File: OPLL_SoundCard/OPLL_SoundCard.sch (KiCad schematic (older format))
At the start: 19 parts, among them P1 Digital, P10 CONN_01X01, P11 CONN_01X01, P12 CONN_01X01, P13 CONN_01X01, P2 Power, P3 Analog, P4 Analog, P5 PWM, P6 PWM, P7 Communication, P8 CONN_01X01, P9 CONN_01X01

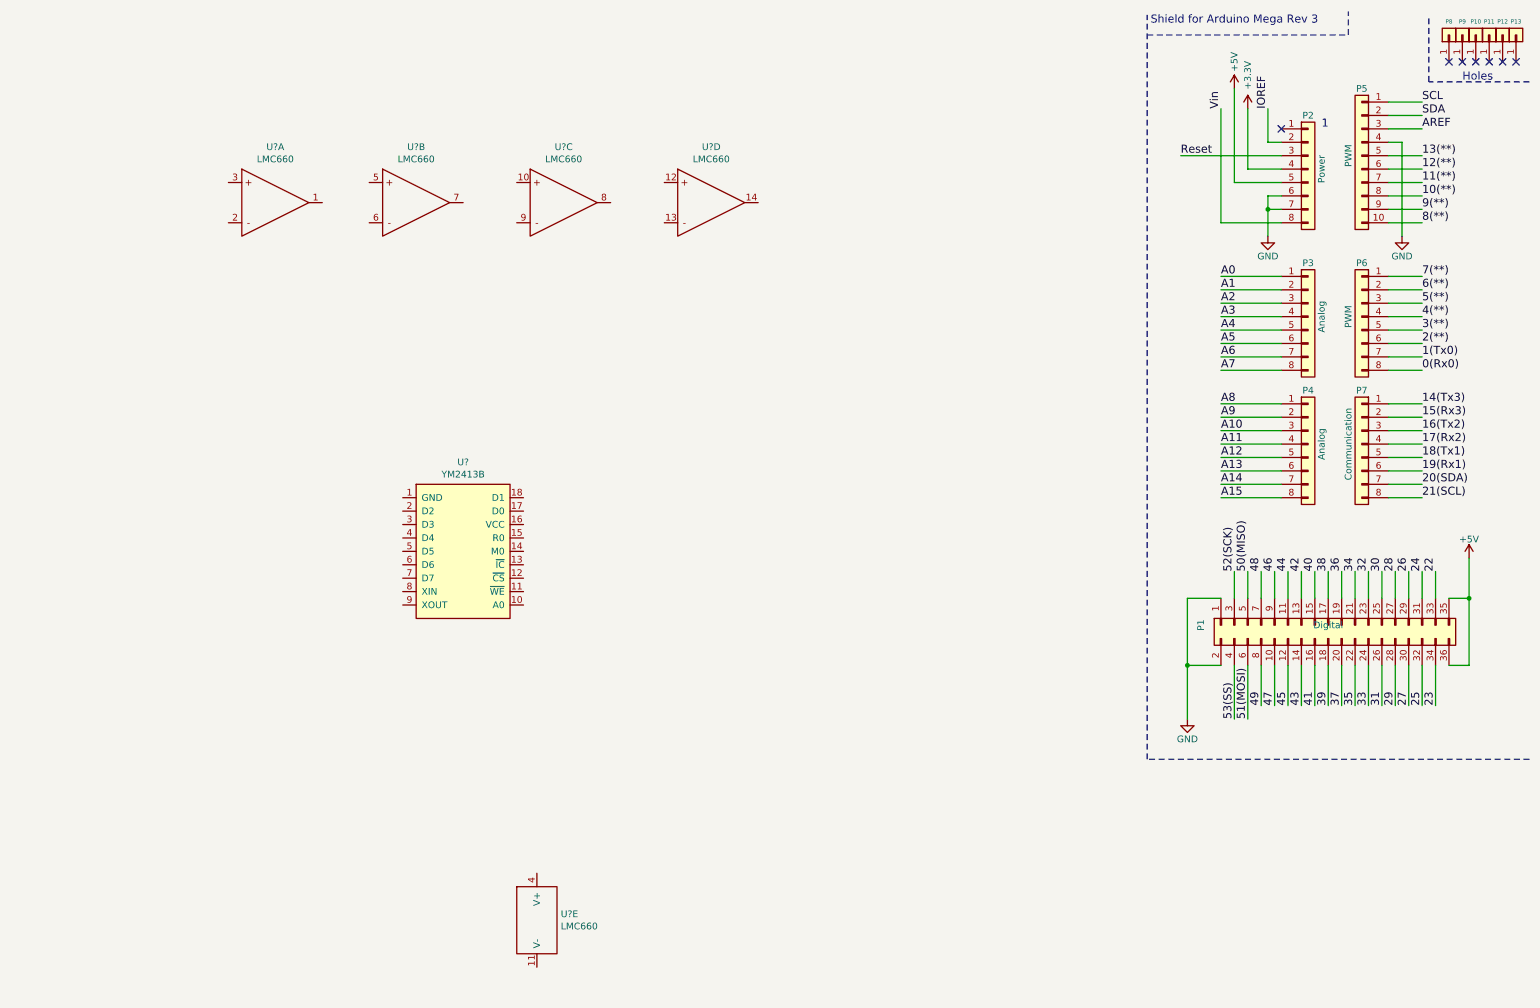
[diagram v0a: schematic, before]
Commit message: 15.12.2020 - Lecture - OPLL schema done
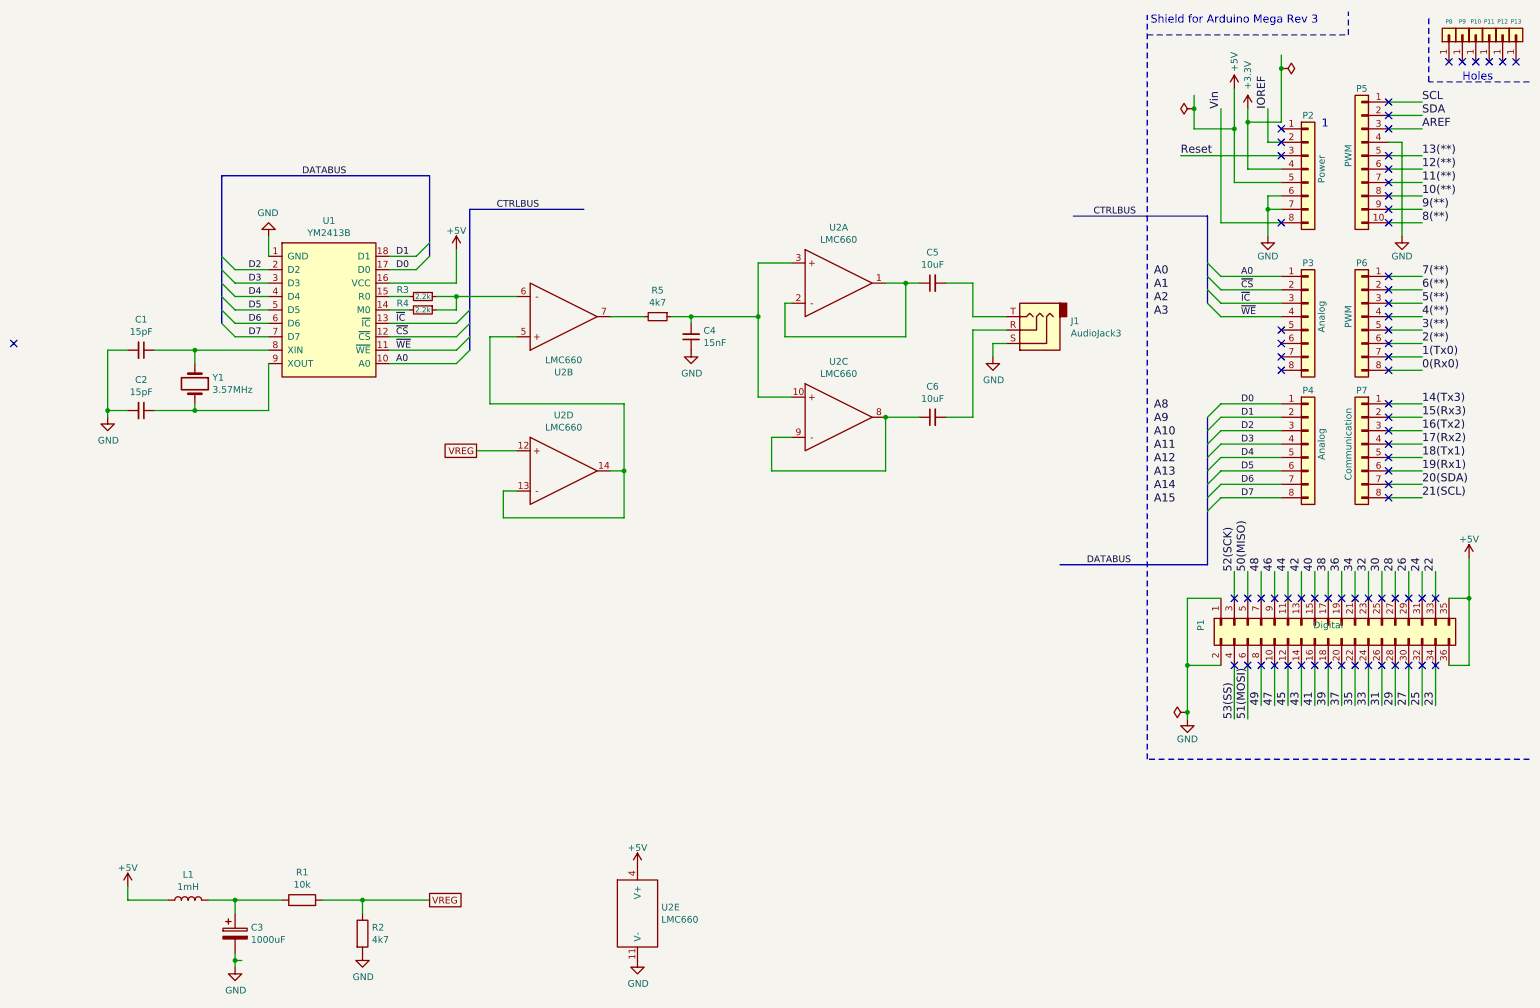
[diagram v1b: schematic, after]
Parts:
- removed U?: LMC660, Package_SO:SOIC-14_3.9x8.7mm_P1.27mm, symbol LMC:LMC660
- added C1, C2: 15pF, symbol Device:C_Small
- added C3: 1000uF, symbol Device:CP
- added C4: 15nF, symbol Device:C_Small
- added C5, C6: 10uF, symbol Device:C_Small
- added J1: AudioJack3, symbol Connector:AudioJack3
- added L1: 1mH, symbol Device:L
- added R1: 10k, symbol Device:R
- added R2: 4k7, symbol Device:R
- added R3, R4: 2.2k, symbol Device:R_Small
- added R5: 4k7, symbol Device:R_Small
- added unit 3 of U2
- added Y1: 3.57MHz, symbol Device:Crystal
- gave numbers to parts that had none: 2
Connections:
- net +5V: now also U1.16 (VCC), U2.4 (V+), L1.1
- net A0: now also U1.10 (A0)
- net A1: no longer P3.2 (Pin_2)
- net A10: no longer P4.3 (Pin_3)
- net A11: no longer P4.4 (Pin_4)
- net A12: no longer P4.5 (Pin_5)
- net A13: no longer P4.6 (Pin_6)
- net A14: no longer P4.7 (Pin_7)
- net A15: no longer P4.8 (Pin_8)
- net A2: no longer P3.3 (Pin_3)
- net A3: no longer P3.4 (Pin_4)
- net A8: no longer P4.1 (Pin_1)
- net A9: no longer P4.2 (Pin_2)
- net GND: now also U1.1 (GND), U2.11 (V-), C1.2, C2.2, C3.2, C4.1, J1.S, R2.2
- net at U2.1: now also U2.2, C5.1
- net at U2.3: now also C4.2, R5.1, U2.10
- net at U2.5: now also U2.13, U2.14
- net at U2.6: now also R3.1, R4.1
- net at U2.7: now also R5.2
- net VREG: now reaches U2.12
- net VREG: now also R1.2, R2.1
- net ~WE: now reaches U1.11 (~WE)
- net ~WE: now also P3.4 (Pin_4)
- net ~CS: now reaches U1.12 (~CS)
- net ~CS: now also P3.2 (Pin_2)
- net ~IC: now reaches U1.13 (~IC)
- net ~IC: now also P3.3 (Pin_3)
- net at U1.14 (M0): now also R4.2
- net at U1.15 (R0): now also R3.2
- net D0: now reaches U1.17 (D0)
- net D0: now also P4.1 (Pin_1)
- net D1: now reaches U1.18 (D1)
- net D1: now also P4.2 (Pin_2)
- net D2: now reaches U1.2 (D2)
- net D2: now also P4.3 (Pin_3)
- net D3: now reaches U1.3 (D3)
- net D3: now also P4.4 (Pin_4)
- net D4: now reaches U1.4 (D4)
- net D4: now also P4.5 (Pin_5)
- net D5: now reaches U1.5 (D5)
- net D5: now also P4.6 (Pin_6)
- net D6: now reaches U1.6 (D6)
- net D6: now also P4.7 (Pin_7)
- net D7: now reaches U1.7 (D7)
- net D7: now also P4.8 (Pin_8)
- net at U1.8 (XIN): now also C1.1, Y1.1
- net at U1.9 (XOUT): now also C2.1, Y1.2
- net A4: no longer names the net of P3.5 (Pin_5)
- net A5: no longer names the net of P3.6 (Pin_6)
- net A6: no longer names the net of P3.7 (Pin_7)
- net A7: no longer names the net of P3.8 (Pin_8)
- new net: C6.1, U2.8, U2.9
- new net: C6.2, J1.R
- new net: C5.2, J1.T
- new net: C3.1, L1.2, R1.1
- no-connect marks 7 -> 72
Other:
- moved on the sheet: U1, U2A, U2B, U2D, U2E

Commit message: mapping
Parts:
- added C7, C8: .1uF, Capacitor_SMD:C_0805_2012Metric_Pad1.18x1.45mm_HandSolder, symbol Device:C_Small
- C1, C2, C4, C5, C6: footprint (none) -> Capacitor_SMD:C_0805_2012Metric_Pad1.18x1.45mm_HandSolder
- C3: footprint (none) -> Capacitor_SMD:C_Elec_10x10.2
- J1: footprint (none) -> Connector_Audio:Jack_3.5mm_PJ320D_Horizontal
- L1: footprint (none) -> Inductor_SMD:L_0805_2012Metric_Pad1.05x1.20mm_HandSolder
- R1, R2, R3, R4, R5: footprint (none) -> Resistor_SMD:R_0805_2012Metric_Pad1.20x1.40mm_HandSolder
- Y1: footprint (none) -> Crystal:Crystal_SMD_HC49-SD_HandSoldering
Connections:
- net +5V: now also C7.1, C8.1
- net GND: now also C7.2, C8.2
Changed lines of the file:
@@
 F 0 "Y1" V 1204 3381 50  0000 L CNN
 F 1 "3.57MHz" V 1295 3381 50  0000 L CNN
-F 2 "" H 1250 3250 50  0001 C CNN
+F 2 "Crystal:Crystal_SMD_HC49-SD_HandSoldering" H 1250 3250 50  0001 C CNN
 F 3 "~" H 1250 3250 50  0001 C CNN
 	1    1250 3250
@@
 F 0 "C1" V 621 3000 50  0000 C CNN
 F 1 "15pF" V 712 3000 50  0000 C CNN
-F 2 "" H 850 3000 50  0001 C CNN
+F 2 "Capacitor_SMD:C_0805_2012Metric_Pad1.18x1.45mm_HandSolder" H 850 3000 50  0001 C CNN
 F 3 "~" H 850 3000 50  0001 C CNN
 	1    850  3000
@@
 F 0 "C2" V 621 3450 50  0000 C CNN
 F 1 "15pF" V 712 3450 50  0000 C CNN
-F 2 "" H 850 3450 50  0001 C CNN
+F 2 "Capacitor_SMD:C_0805_2012Metric_Pad1.18x1.45mm_HandSolder" H 850 3450 50  0001 C CNN
 F 3 "~" H 850 3450 50  0001 C CNN
 	1    850  3450
@@
 F 0 "R4" V 2900 2550 50  0000 C CNN
 F 1 "2.2k" V 2950 2700 39  0000 C CNN
-F 2 "" H 2950 2700 50  0001 C CNN
+F 2 "Resistor_SMD:R_0805_2012Metric_Pad1.20x1.40mm_HandSolder" H 2950 2700 50  0001 C CNN
 F 3 "~" H 2950 2700 50  0001 C CNN
 	1    2950 2700
@@
 F 0 "R3" V 2900 2450 50  0000 C CNN
 F 1 "2.2k" V 2950 2600 39  0000 C CNN
-F 2 "" H 2950 2600 50  0001 C CNN
+F 2 "Resistor_SMD:R_0805_2012Metric_Pad1.20x1.40mm_HandSolder" H 2950 2600 50  0001 C CNN
 F 3 "~" H 2950 2600 50  0001 C CNN
 	1    2950 2600
@@
 F 0 "R5" V 4504 2750 50  0000 C CNN
 F 1 "4k7" V 4595 2750 50  0000 C CNN
-F 2 "" H 4700 2750 50  0001 C CNN
+F 2 "Resistor_SMD:R_0805_2012Metric_Pad1.20x1.40mm_HandSolder" H 4700 2750 50  0001 C CNN
 F 3 "~" H 4700 2750 50  0001 C CNN
 	1    4700 2750
@@
 F 0 "C4" H 4858 2854 50  0000 R CNN
 F 1 "15nF" H 4858 2945 50  0000 R CNN
-F 2 "" H 4950 2900 50  0001 C CNN
+F 2 "Capacitor_SMD:C_0805_2012Metric_Pad1.18x1.45mm_HandSolder" H 4950 2900 50  0001 C CNN
 F 3 "~" H 4950 2900 50  0001 C CNN
 	1    4950 2900
@@
 F 0 "C6" V 6979 3500 50  0000 C CNN
 F 1 "10uF" V 6888 3500 50  0000 C CNN
-F 2 "" H 6750 3500 50  0001 C CNN
+F 2 "Capacitor_SMD:C_0805_2012Metric_Pad1.18x1.45mm_HandSolder" H 6750 3500 50  0001 C CNN
 F 3 "~" H 6750 3500 50  0001 C CNN
 	1    6750 3500
@@
 F 0 "C5" V 6979 2500 50  0000 C CNN
 F 1 "10uF" V 6888 2500 50  0000 C CNN
-F 2 "" H 6750 2500 50  0001 C CNN
+F 2 "Capacitor_SMD:C_0805_2012Metric_Pad1.18x1.45mm_HandSolder" H 6750 2500 50  0001 C CNN
 F 3 "~" H 6750 2500 50  0001 C CNN
 	1    6750 2500
@@
 F 0 "J1" H 7220 2783 50  0000 R CNN
 F 1 "AudioJack3" H 7220 2874 50  0000 R CNN
-F 2 "" H 7500 2850 50  0001 C CNN
+F 2 "Connector_Audio:Jack_3.5mm_PJ320D_Horizontal" H 7500 2850 50  0001 C CNN
 F 3 "~" H 7500 2850 50  0001 C CNN
 	1    7500 2850
@@
 F 0 "L1" V 1390 7100 50  0000 C CNN
 F 1 "1mH" V 1299 7100 50  0000 C CNN
-F 2 "" H 1200 7100 50  0001 C CNN
+F 2 "Inductor_SMD:L_0805_2012Metric_Pad1.05x1.20mm_HandSolder" H 1200 7100 50  0001 C CNN
 F 3 "~" H 1200 7100 50  0001 C CNN
 	1    1200 7100
@@
 F 0 "C3" H 1668 7396 50  0000 L CNN
 F 1 "1000uF" H 1668 7305 50  0000 L CNN
-F 2 "" H 1588 7200 50  0001 C CNN
+F 2 "Capacitor_SMD:C_Elec_10x10.2" H 1588 7200 50  0001 C CNN
 F 3 "~" H 1550 7350 50  0001 C CNN
 	1    1550 7350
@@
 F 0 "R1" V 2257 7100 50  0000 C CNN
 F 1 "10k" V 2166 7100 50  0000 C CNN
-F 2 "" V 1980 7100 50  0001 C CNN
+F 2 "Resistor_SMD:R_0805_2012Metric_Pad1.20x1.40mm_HandSolder" V 1980 7100 50  0001 C CNN
 F 3 "~" H 2050 7100 50  0001 C CNN
 	1    2050 7100
@@
 F 0 "R2" H 2570 7396 50  0000 L CNN
 F 1 "4k7" H 2570 7305 50  0000 L CNN
-F 2 "" V 2430 7350 50  0001 C CNN
+F 2 "Resistor_SMD:R_0805_2012Metric_Pad1.20x1.40mm_HandSolder" V 2430 7350 50  0001 C CNN
 F 3 "~" H 2500 7350 50  0001 C CNN
 	1    2500 7350
@@
 Wire Wire Line
 	8700 1200 8700 1100
-Wire Bus Line
-	3000 1700 3000 2300
-Wire Bus Line
-	3300 1950 3300 3000
-Wire Bus Line
-	8800 2000 8800 2650
-Wire Bus Line
-	1450 1700 1450 2800
-Wire Bus Line
-	8800 3500 8800 4600
 $Comp
 L power:PWR_FLAG #FLG0101
@@
 Wire Wire Line
 	8650 5700 8650 5750
+$Comp
+L Device:C_Small C7
+U 1 1 5FDD9836
+P 5550 7200
+F 0 "C7" V 5779 7200 50  0000 C CNN
+F 1 ".1uF" V 5688 7200 50  0000 C CNN
+F 2 "Capacitor_SMD:C_0805_2012Metric_Pad1.18x1.45mm_HandSolder" H 5550 7200 50  0001 C CNN
+F 3 "~" H 5550 7200 50  0001 C CNN
+	1    5550 7200
+	1    0    0    -1
+$EndComp
+$Comp
+L power:GND #PWR08
+U 1 1 5FDD9FAF
+P 5550 7300
+F 0 "#PWR08" H 5550 7050 50  0001 C CNN
+F 1 "GND" H 5555 7127 50  0000 C CNN
+F 2 "" H 5550 7300 50  0001 C CNN
+F 3 "" H 5550 7300 50  0001 C CNN
+	1    5550 7300
+	1    0    0    -1
+$EndComp
+$Comp
+L power:+5V #PWR07
+U 1 1 5FDDA552
+P 5550 7100
+F 0 "#PWR07" H 5550 6950 50  0001 C CNN
+F 1 "+5V" H 5550 7240 50  0000 C CNN
+F 2 "" H 5550 7100 50  0000 C CNN
+F 3 "" H 5550 7100 50  0000 C CNN
+	1    5550 7100
+	1    0    0    -1
+$EndComp
+$Comp
+L Device:C_Small C8
+U 1 1 5FDDC365
+P 6150 7200
+F 0 "C8" V 6379 7200 50  0000 C CNN
+F 1 ".1uF" V 6288 7200 50  0000 C CNN
+F 2 "Capacitor_SMD:C_0805_2012Metric_Pad1.18x1.45mm_HandSolder" H 6150 7200 50  0001 C CNN
+F 3 "~" H 6150 7200 50  0001 C CNN
+	1    6150 7200
+	1    0    0    -1
+$EndComp
+$Comp
+L power:GND #PWR010
+U 1 1 5FDDC36B
+P 6150 7300
+F 0 "#PWR010" H 6150 7050 50  0001 C CNN
+F 1 "GND" H 6155 7127 50  0000 C CNN
+F 2 "" H 6150 7300 50  0001 C CNN
+F 3 "" H 6150 7300 50  0001 C CNN
+	1    6150 7300
+	1    0    0    -1
+$EndComp
+$Comp
+L power:+5V #PWR09
+U 1 1 5FDDC371
+P 6150 7100
+F 0 "#PWR09" H 6150 6950 50  0001 C CNN
+F 1 "+5V" H 6150 7240 50  0000 C CNN
+F 2 "" H 6150 7100 50  0000 C CNN
+F 3 "" H 6150 7100 50  0000 C CNN
+	1    6150 7100
+	1    0    0    -1
+$EndComp
+Wire Bus Line
+	3000 1700 3000 2300
+Wire Bus Line
+	3300 1950 3300 3000
+Wire Bus Line
+	8800 2000 8800 2650
+Wire Bus Line
+	1450 1700 1450 2800
+Wire Bus Line
+	8800 3500 8800 4600
 $EndSCHEMATC
